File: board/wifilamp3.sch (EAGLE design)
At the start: 7 parts

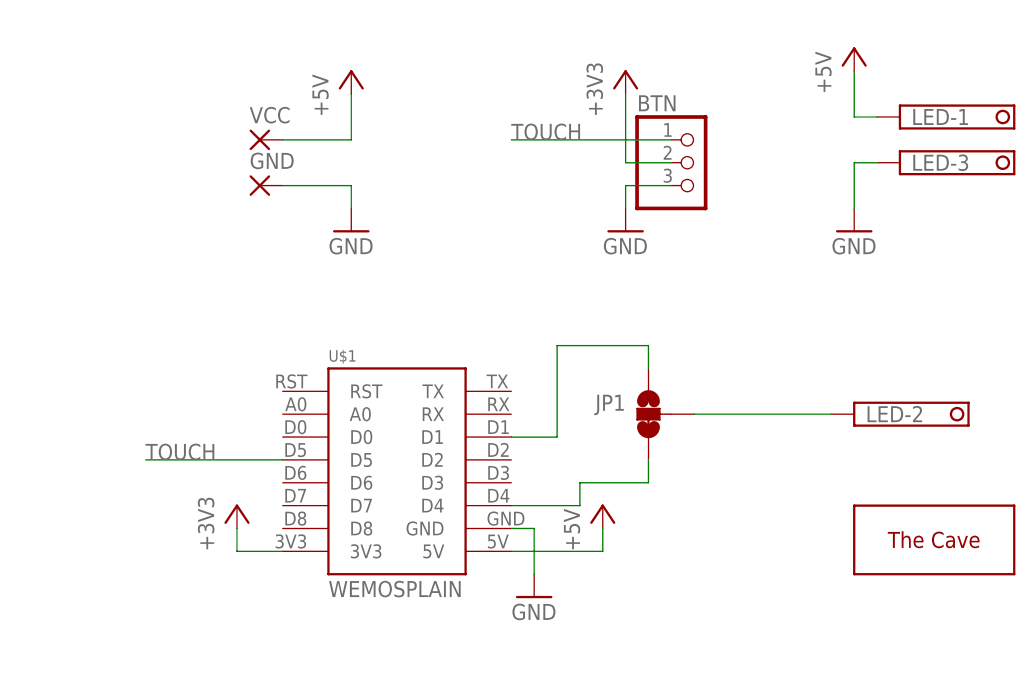
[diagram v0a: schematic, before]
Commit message: [Board] Update to rev3
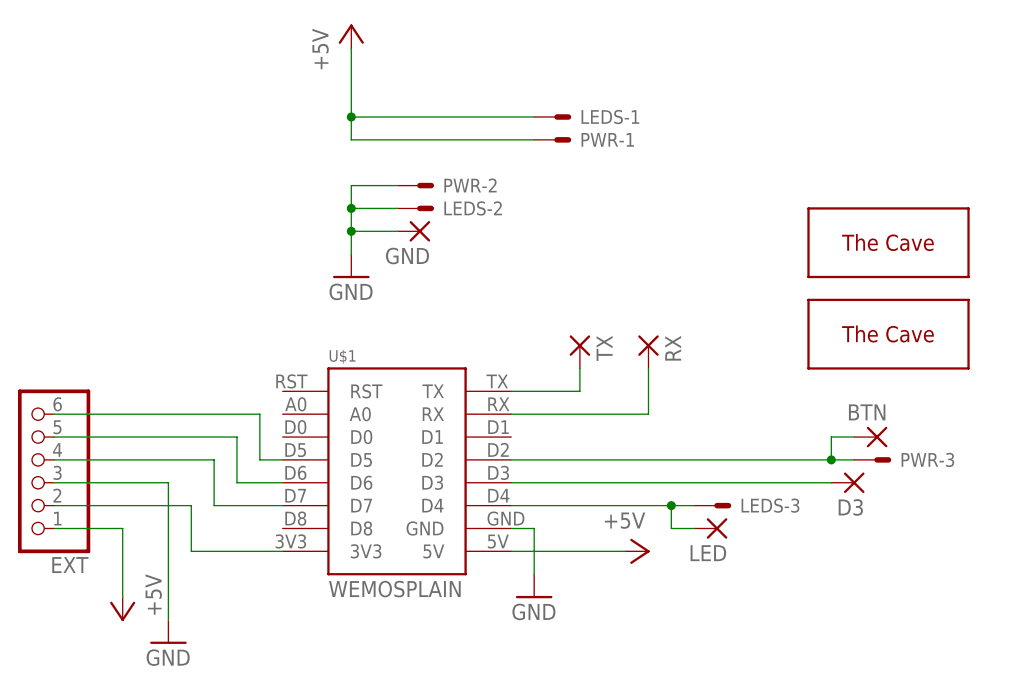
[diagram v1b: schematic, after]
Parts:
- removed JP1: JUMPER-SMT_3_1-NC_TRACE_NO-SILK, SparkFun-Jumpers:JUMPER-SMT_3_1-NC_TRACE_NO-SILK
- removed VCC: PAD3,81/2, thecave:PAD3,81/2
- added D3, RX, TX: WIREPADSMD1,27-254, wirepad:WIREPADSMD1,27-254
- added EXT: (no value), pinhead:PINHD-1X6
- added LEDS, PWR: JST-XH-03-PIN-LONG-PAD, Rembrandt Electronics - JST XH Connectors v1-0:JST-XH-03-PIN-LONG-PAD
- added U$3: THECAVE_LOGO_BOTTOM_MEDIUM, thecave:THECAVE_LOGO_BOTTOM_MEDIUM
- BTN: value (none) -> WIREPADSMD1,27-254; device pinhead:PINHD-1X3 -> wirepad:WIREPADSMD1,27-254
- GND: value WIREPAD3,81/1,4 -> WIREPADSMD1,27-254; device wirepad:WIREPAD3,81/1,4 -> wirepad:WIREPADSMD1,27-254
- LED: value 1751251 -> WIREPADSMD1,27-254; device con-phoenix-350:1751251 -> wirepad:WIREPADSMD1,27-254
- U$2: value THECAVE_LOGO_TOP_SMALL -> THECAVE_LOGO_TOP_MEDIUM; device thecave:THECAVE_LOGO_TOP_SMALL -> thecave:THECAVE_LOGO_TOP_MEDIUM
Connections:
- removed net +3V3: BTN.2, U$1.3V3
- removed net TOUCH: BTN.1, U$1.D5
- new net N$4: EXT.2, U$1.3V3
- new net N$5: EXT.4, U$1.D7
- new net N$6: EXT.5, U$1.D6
- new net N$7: EXT.6, U$1.D5
- new net N$8: RX.P, U$1.RX
- new net N$9: D3.P, U$1.D3
- net +5V: now also EXT.1, LEDS-1.S, PWR-1.S; no longer LED-1.K, VCC.P
- net GND: now also EXT.3, LEDS-2.S, PWR-2.S; no longer BTN.3, LED-3.K
- net N$1: now also LED.P, LEDS-3.S, U$1.D4; no longer JP1.1, U$1.D1
- net N$2: now also BTN.P, PWR-3.S, U$1.D2; no longer JP1.3, U$1.D4
- net N$3: now also TX.P, U$1.TX; no longer JP1.2, LED-2.K
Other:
- moved on the sheet: GND
